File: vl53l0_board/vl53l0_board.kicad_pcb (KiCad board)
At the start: 4 copper layers, 5 x 3 mm, 3 parts, among them J17 Conn_01x05, U7 VL53L0X

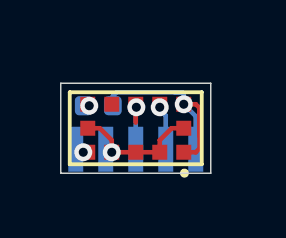
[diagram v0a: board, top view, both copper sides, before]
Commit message: Update DC motor holder model
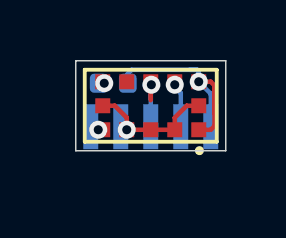
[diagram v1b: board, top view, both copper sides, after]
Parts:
- moved J17 0.90 mm to (0.00, -1.75)
- moved R13 0.90 mm to (-1.25, -2.20)
- moved U7 0.90 mm to (0.00, -1.45)
